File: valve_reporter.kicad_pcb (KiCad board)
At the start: 2 copper layers, 52 parts, among them J1 Screw_Terminal_01x05, J2 Screw_Terminal_01x14, K1 G5LE-1, Q1 2N3904, U1 NodeMCU_1.0_(ESP-12E), U2 MC7805CTG

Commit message: Schematic is shaping up
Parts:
- added H5: MountingHole_Pad, MountingHole:MountingHole_3.2mm_M3_ISO7380_Pad, F.Cu at (136.0, 129.6)
- added H6: MountingHole_Pad, MountingHole:MountingHole_3.2mm_M3_ISO7380_Pad, F.Cu at (110.6, 77.6)
- added H7: MountingHole_Pad, MountingHole:MountingHole_3.2mm_M3_ISO7380_Pad, F.Cu at (136.0, 77.5)
- added H8: MountingHole_Pad, MountingHole:MountingHole_3.2mm_M3_ISO7380_Pad, F.Cu at (110.6, 129.7)
- D3, D4, D5, D6, D7, D8, D9: footprint Diode_SMD:D_SOD-323F -> Diode_SMD:D_SOD-323_HandSoldering
- J1: footprint TerminalBlock_Phoenix:TerminalBlock_Phoenix_PT-1,5-5-5.0-H_1x05_P5.00mm_Horizontal -> TerminalBlock_Phoenix:TerminalBlock_Phoenix_PT-1,5-5-5.0-H_1x05_P5.00mm_Horizontal_valve_rep
- J2: footprint TerminalBlock_Phoenix:TerminalBlock_Phoenix_PT-1,5-14-3.5-H_1x14_P3.50mm_Horizontal -> TerminalBlock_Phoenix:TerminalBlock_Phoenix_PT-1,5-14-3.5-H_1x14_P3.50mm_Horizontal_valve_rep
- moved U2 99.1 mm to (102.9, 121.9), turned to 270 degrees
- moved H2 94.5 mm to (86.4, 134.6)
- moved D1 88.0 mm to (95.2, 134.1), turned to 270 degrees
- moved H3 76.0 mm to (86.4, 73.7)
- moved C9 70.2 mm to (105.4, 134.0), turned to 270 degrees
- moved Q1 69.9 mm to (103.9, 100.7), turned to 180 degrees
- moved R1 68.8 mm to (100.3, 134.0), turned to 90 degrees
- moved R17 68.8 mm to (101.7, 74.9), turned to 180 degrees
- moved R16 68.4 mm to (155.1, 126.3), turned to 180 degrees
- moved R2 67.7 mm to (102.7, 110.5)
- moved C8 64.0 mm to (102.7, 115.6)
- moved J2 56.6 mm to (170.2, 127.0), turned to 90 degrees
- moved J1 55.3 mm to (88.9, 104.8), turned to 270 degrees
- moved R7 46.2 mm to (142.2, 113.0), turned to 90 degrees
- moved D2 45.9 mm to (102.7, 106.7)
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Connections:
- net Net-(J1-Pad3) renamed /RelOn
- net Net-(J1-Pad4) renamed /RelOff
- net Net-(J1-Pad5) renamed /RelIn
- J2 pad 1: +12V -> Net-(D16-Pad1)
- J2 pad 10: Net-(D14-Pad1) -> +12V
- J2 pad 11: +12V -> Net-(D11-Pad1)
- J2 pad 12: Net-(D15-Pad1) -> +12V
- J2 pad 13: +12V -> Net-(D10-Pad1)
- J2 pad 14: Net-(D16-Pad1) -> +12V
- J2 pad 2: Net-(D10-Pad1) -> +12V
- J2 pad 3: +12V -> Net-(D15-Pad1)
- J2 pad 4: Net-(D11-Pad1) -> +12V
- J2 pad 5: +12V -> Net-(D14-Pad1)
- J2 pad 6: Net-(D12-Pad1) -> +12V
- J2 pad 7: +12V -> Net-(D13-Pad1)
- J2 pad 8: Net-(D13-Pad1) -> +12V
- J2 pad 9: +12V -> Net-(D12-Pad1)
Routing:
- net +12V: track 0.00 -> 178.0 mm
- net Net-(C1-Pad1): track 0.00 -> 56.2 mm
- net /RelIn: track 0.00 -> 43.9 mm
- net /RelOff: track 0.00 -> 39.8 mm
- net Net-(R2-Pad2): track 0.00 -> 34.1 mm
- net Net-(C7-Pad1): track 0.00 -> 32.3 mm
- net Net-(D2-Pad2): track 0.00 -> 29.8 mm
- net Net-(C6-Pad1): track 0.00 -> 28.9 mm
- net Net-(C4-Pad1): track 0.00 -> 23.3 mm
- net Net-(C5-Pad1): track 0.00 -> 23.0 mm
- net /RelOn: track 0.00 -> 22.8 mm
- net +5V: track 0.00 -> 21.5 mm
- net Net-(C3-Pad1): track 0.00 -> 20.5 mm
- net Net-(C2-Pad1): track 0.00 -> 17.9 mm
- net Net-(D12-Pad1): track 0.00 -> 15.0 mm
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- added copper zone on B.Cu, net GND
- added copper zone on F.Cu, net GND
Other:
- board outline added: 96.5 x 71.1 mm
- net class Power added: clearance 0.2, trace_width 0.75, via_dia 0.8, via_drill 0.4
- net class Relay added: clearance 0.8, trace_width 1, via_dia 0.8, via_drill 0.4
- board text added: "GSV"
- board text added: "Lou Vervecken 01/19"
- board text added: "Valve Reporter 1.0"

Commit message: Add outputs
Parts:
- added G***: LOGO, artwork:m_vac, F.Cu at (157.5, 74.9)

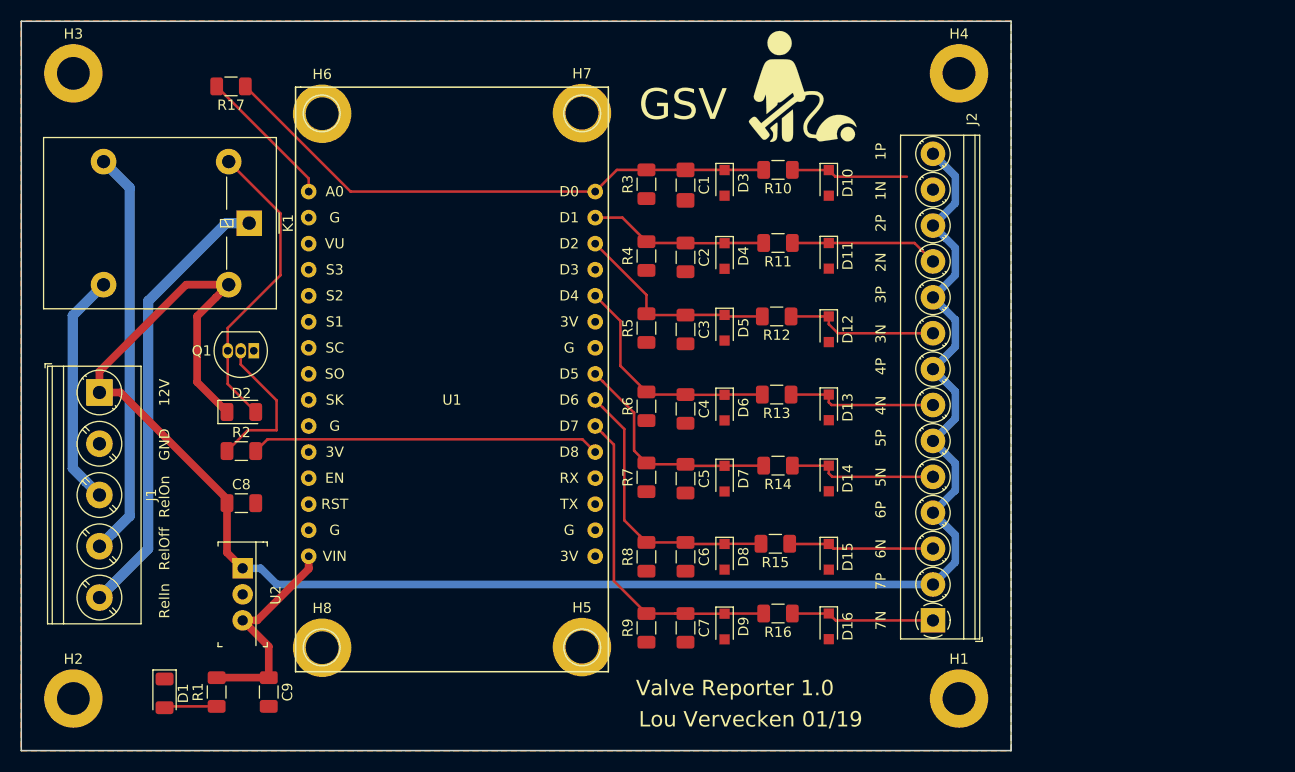
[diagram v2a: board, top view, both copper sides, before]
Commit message: Fixed non connect and increased keepout
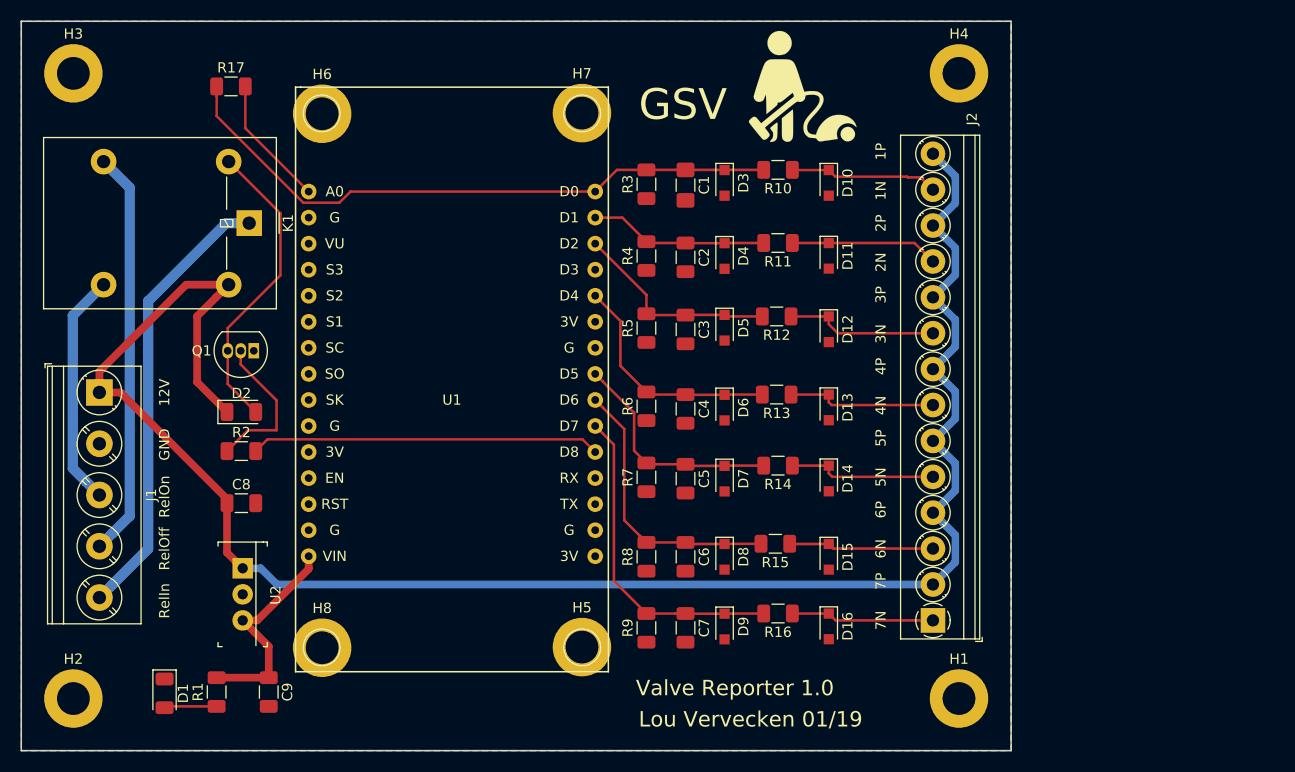
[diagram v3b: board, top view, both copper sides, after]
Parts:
- turned R17 to 0 degrees
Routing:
- net Net-(C1-Pad1): track 56.2 -> 61.6 mm
- net Net-(D10-Pad1): track 11.4 -> 14.5 mm
- net Net-(R17-Pad2): track 14.0 -> 12.8 mm
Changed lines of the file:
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@@
     (thickness 1.6)
     (drawings 7)
-    (tracks 183)
+    (tracks 190)
     (zones 0)
     (modules 57)
@@
   )
   (module Resistor_SMD:R_1206_3216Metric (layer F.Cu)
-    (at 101.73 74.93 180)
+    (at 101.73 74.93)
     (descr "Resistor SMD 1206 (3216 Metric), square (rectangular) end terminal, IPC_7351 nominal, (Body size source: http://www.tortai-tech.com/upload/download/2011102023233369053.pdf), generated with kicad-footprint-generator")
     (tags resistor)
     (attr smd)
-    (fp_text reference R17 (at 0 -1.82 180) (layer F.SilkS)
-      (effects (font (size 1 1) (thickness 0.15)))
-    )
-    (fp_text value 0 (at 0 1.82 180) (layer F.Fab)
-      (effects (font (size 1 1) (thickness 0.15)))
-    )
-    (fp_text user %R (at 0 0 180) (layer F.Fab)
+    (fp_text reference R17 (at 0 -1.82) (layer F.SilkS)
+      (effects (font (size 1 1) (thickness 0.15)))
+    )
+    (fp_text value 0 (at 0 1.82) (layer F.Fab)
+      (effects (font (size 1 1) (thickness 0.15)))
+    )
+    (fp_text user %R (at 0 0) (layer F.Fab)
       (effects (font (size 0.8 0.8) (thickness 0.12)))
     )
@@
     (fp_line (start -1.6 -0.8) (end 1.6 -0.8) (layer F.Fab) (width 0.1))
     (fp_line (start -1.6 0.8) (end -1.6 -0.8) (layer F.Fab) (width 0.1))
-    (pad 2 smd roundrect (at 1.4 0 180) (size 1.25 1.75) (layers F.Cu F.Paste F.Mask) (roundrect_rratio 0.2)
+    (pad 2 smd roundrect (at 1.4 0) (size 1.25 1.75) (layers F.Cu F.Paste F.Mask) (roundrect_rratio 0.2)
       (net 22 "Net-(R17-Pad2)"))
-    (pad 1 smd roundrect (at -1.4 0 180) (size 1.25 1.75) (layers F.Cu F.Paste F.Mask) (roundrect_rratio 0.2)
+    (pad 1 smd roundrect (at -1.4 0) (size 1.25 1.75) (layers F.Cu F.Paste F.Mask) (roundrect_rratio 0.2)
       (net 1 "Net-(C1-Pad1)"))
     (model ${KISYS3DMOD}/Resistor_SMD.3dshapes/R_1206_3216Metric.wrl
@@
   (segment (start 139.360002 83.07) (end 137.245001 85.185001) (width 0.25) (layer F.Cu) (net 1))
   (segment (start 142.24 83.07) (end 139.360002 83.07) (width 0.25) (layer F.Cu) (net 1))
-  (segment (start 113.385001 85.185001) (end 103.13 74.93) (width 0.25) (layer F.Cu) (net 1))
   (segment (start 137.245001 85.185001) (end 113.385001 85.185001) (width 0.25) (layer F.Cu) (net 1))
   (segment (start 149.88 83.07) (end 149.86 83.09) (width 0.25) (layer F.Cu) (net 1))
@@
   (segment (start 149.84 83.07) (end 149.86 83.09) (width 0.25) (layer F.Cu) (net 1))
   (segment (start 146.05 83.07) (end 149.84 83.07) (width 0.25) (layer F.Cu) (net 1))
+  (segment (start 100.33 75.905) (end 100.33 74.93) (width 0.25) (layer F.Cu) (net 1))
+  (segment (start 100.33 77.818762) (end 100.33 75.905) (width 0.25) (layer F.Cu) (net 1))
+  (segment (start 108.78324 86.272002) (end 100.33 77.818762) (width 0.25) (layer F.Cu) (net 1))
+  (segment (start 112.298 86.272002) (end 108.78324 86.272002) (width 0.25) (layer F.Cu) (net 1))
+  (segment (start 113.385001 85.185001) (end 112.298 86.272002) (width 0.25) (layer F.Cu) (net 1))
   (segment (start 150.03 90.2) (end 149.86 90.37) (width 0.25) (layer F.Cu) (net 3))
   (segment (start 146.22 90.37) (end 146.05 90.2) (width 0.25) (layer F.Cu) (net 3))
@@
   (segment (start 156.49 83.09) (end 156.47 83.07) (width 0.25) (layer F.Cu) (net 13))
   (segment (start 160.02 83.09) (end 156.49 83.09) (width 0.25) (layer F.Cu) (net 13))
+  (segment (start 167.710001 83.800001) (end 167.64 83.73) (width 0.25) (layer F.Cu) (net 13))
+  (segment (start 168.980001 83.800001) (end 167.710001 83.800001) (width 0.25) (layer F.Cu) (net 13))
+  (segment (start 170.18 85) (end 168.980001 83.800001) (width 0.25) (layer F.Cu) (net 13))
   (segment (start 168.38 90.2) (end 160.02 90.2) (width 0.25) (layer F.Cu) (net 14))
   (segment (start 170.18 92) (end 168.38 90.2) (width 0.25) (layer F.Cu) (net 14))
@@
   (segment (start 136.007 109.347) (end 137.245001 110.585001) (width 0.25) (layer F.Cu) (net 21))
   (segment (start 105.283 109.347) (end 136.007 109.347) (width 0.25) (layer F.Cu) (net 21))
-  (segment (start 109.305001 83.905001) (end 100.33 74.93) (width 0.25) (layer F.Cu) (net 22))
-  (segment (start 109.305001 85.185001) (end 109.305001 83.905001) (width 0.25) (layer F.Cu) (net 22))
+  (segment (start 103.13 79.01) (end 103.13 74.93) (width 0.25) (layer F.Cu) (net 22))
+  (segment (start 109.305001 85.185001) (end 103.13 79.01) (width 0.25) (layer F.Cu) (net 22))
   (segment (start 87.600001 113.475001) (end 88.9 114.775) (width 1) (layer B.Cu) (net 39))
   (segment (start 86.299999 112.174999) (end 87.600001 113.475001) (width 1) (layer B.Cu) (net 39))
@@
     (polygon
       (pts
-        (xy 114.3 83.82) (xy 114.3 68.58) (xy 132.08 68.58) (xy 132.08 83.82)
+        (xy 109.22 83.82) (xy 109.22 68.58) (xy 137.16 68.58) (xy 137.16 83.82)
       )
     )
-  )
-  (zone (net 2) (net_name GND) (layer F.Cu) (hatch edge 0.508)
-    (connect_pads (clearance 0.508))
-    (min_thickness 0.254)
-    (fill yes (arc_segments 16) (thermal_gap 0.508) (thermal_bridge_width 0.508) (smoothing chamfer))
-    (polygon
-      (pts
-        (xy 81.28 68.58) (xy 81.28 139.7) (xy 177.8 139.7) (xy 177.8 68.58)
-      )
-    )

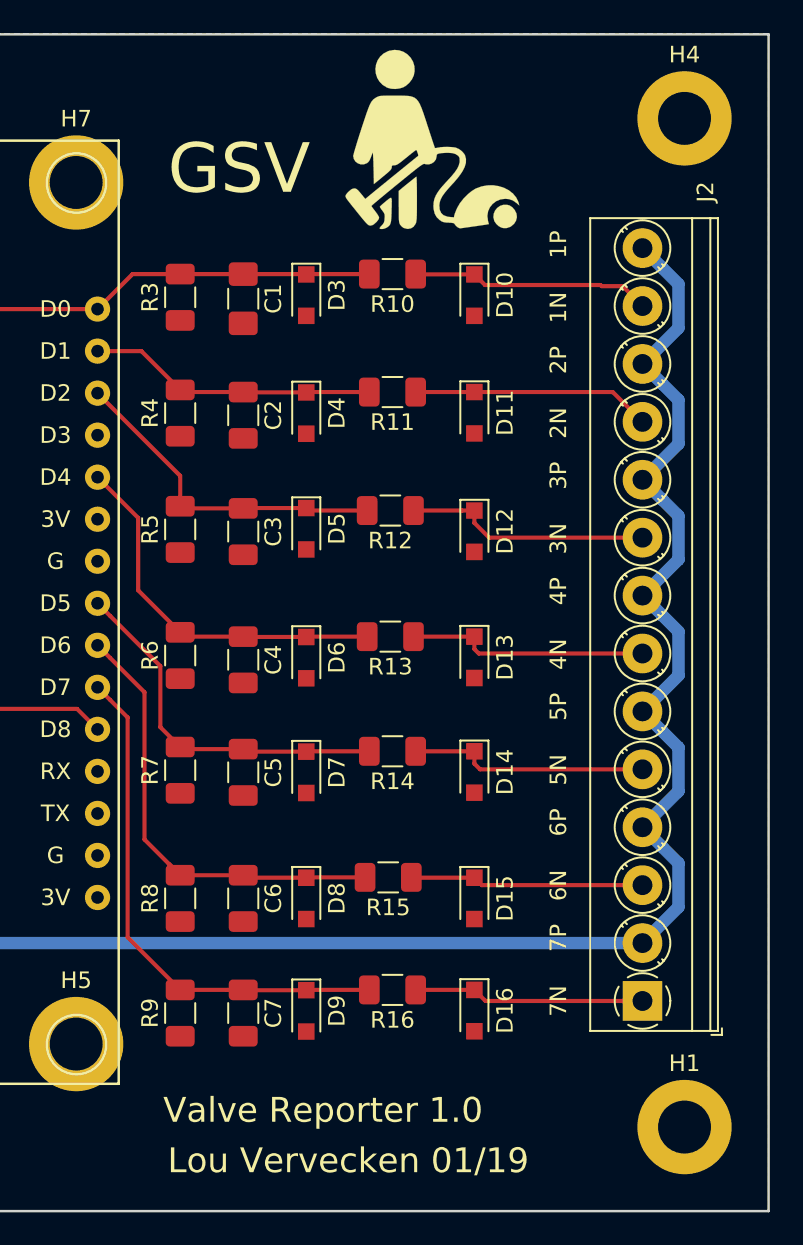
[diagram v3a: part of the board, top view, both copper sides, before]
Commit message: Extra decoupling
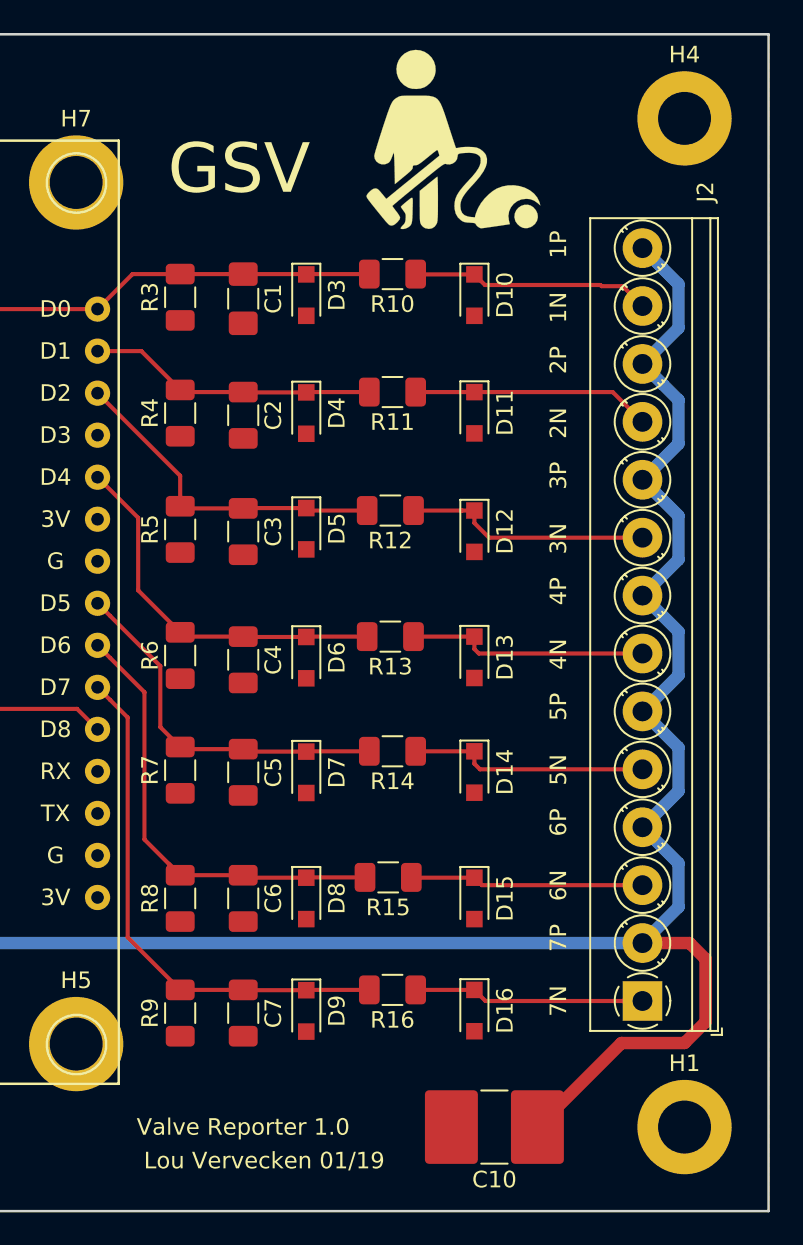
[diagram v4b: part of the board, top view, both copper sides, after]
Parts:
- added C10: 50uF, Capacitor_SMD:C_2816_7142Metric_Pad3.20x4.45mm_HandSolder, F.Cu at (161.2, 134.6)
- moved G*** 1.27 mm to (158.8, 74.9)
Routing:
- net +12V: track 178.0 -> 198.8 mm
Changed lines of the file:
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@@
     (thickness 1.6)
     (drawings 7)
-    (tracks 190)
+    (tracks 196)
     (zones 0)
-    (modules 57)
+    (modules 58)
     (nets 42)
   )
@@
     (add_net /RelOff)
     (add_net /RelOn)
+  )
+  (module Capacitor_SMD:C_2816_7142Metric_Pad3.20x4.45mm_HandSolder (layer F.Cu)
+    (at 161.23 134.62 180)
+    (descr "Capacitor SMD 2816 (7142 Metric), square (rectangular) end terminal, IPC_7351 nominal with elongated pad for handsoldering. (Body size from: https://www.vishay.com/docs/30100/wsl.pdf), generated with kicad-footprint-generator")
+    (tags "capacitor handsolder")
+    (attr smd)
+    (fp_text reference C10 (at 0 -3.18 180) (layer F.SilkS)
+      (effects (font (size 1 1) (thickness 0.15)))
+    )
+    (fp_text value 50uF (at 0 3.18 180) (layer F.Fab)
+      (effects (font (size 1 1) (thickness 0.15)))
+    )
+    (fp_line (start -3.55 2.1) (end -3.55 -2.1) (layer F.Fab) (width 0.1))
+    (fp_line (start -3.55 -2.1) (end 3.55 -2.1) (layer F.Fab) (width 0.1))
+    (fp_line (start 3.55 -2.1) (end 3.55 2.1) (layer F.Fab) (width 0.1))
+    (fp_line (start 3.55 2.1) (end -3.55 2.1) (layer F.Fab) (width 0.1))
+    (fp_line (start -0.797369 -2.21) (end 0.797369 -2.21) (layer F.SilkS) (width 0.12))
+    (fp_line (start -0.797369 2.21) (end 0.797369 2.21) (layer F.SilkS) (width 0.12))
+    (fp_line (start -4.45 2.48) (end -4.45 -2.48) (layer F.CrtYd) (width 0.05))
+    (fp_line (start -4.45 -2.48) (end 4.45 -2.48) (layer F.CrtYd) (width 0.05))
+    (fp_line (start 4.45 -2.48) (end 4.45 2.48) (layer F.CrtYd) (width 0.05))
+    (fp_line (start 4.45 2.48) (end -4.45 2.48) (layer F.CrtYd) (width 0.05))
+    (fp_text user %R (at 0 0 180) (layer F.Fab)
+      (effects (font (size 1 1) (thickness 0.15)))
+    )
+    (pad 1 smd roundrect (at -2.6 0 180) (size 3.2 4.45) (layers F.Cu F.Paste F.Mask) (roundrect_rratio 0.078125)
+      (net 9 +12V))
+    (pad 2 smd roundrect (at 2.6 0 180) (size 3.2 4.45) (layers F.Cu F.Paste F.Mask) (roundrect_rratio 0.078125)
+      (net 2 GND))
+    (model ${KISYS3DMOD}/Capacitor_SMD.3dshapes/C_2816_7142Metric.wrl
+      (at (xyz 0 0 0))
+      (scale (xyz 1 1 1))
+      (rotate (xyz 0 0 0))
+    )
   )
   (module Diode_SMD:D_SOD-323_HandSoldering (layer F.Cu)
@@
   )
   (module artwork:m_vac (layer F.Cu)
-    (at 157.48 74.93)
+    (at 158.75 74.93)
     (fp_text reference G*** (at 0 0) (layer F.SilkS) hide
       (effects (font (size 1.524 1.524) (thickness 0.3)))
@@
       (xy -2.485976 3.533957)) (layer F.SilkS) (width 0.01))
   )
-  (gr_text "Lou Vervecken 01/19" (at 152.4 136.652) (layer F.SilkS)
-    (effects (font (size 1.5 1.5) (thickness 0.3)))
-  )
-  (gr_text "Valve Reporter 1.0" (at 150.876 133.604) (layer F.SilkS)
-    (effects (font (size 1.5 1.5) (thickness 0.3)))
+  (gr_text "Lou Vervecken 01/19" (at 147.32 136.652) (layer F.SilkS)
+    (effects (font (size 1 1) (thickness 0.25)))
+  )
+  (gr_text "Valve Reporter 1.0" (at 146.05 134.62) (layer F.SilkS)
+    (effects (font (size 1 1) (thickness 0.25)))
   )
   (gr_text GSV (at 145.796 76.708) (layer F.SilkS)
@@
   (segment (start 172.355001 86.324999) (end 172.355001 83.675001) (width 0.75) (layer B.Cu) (net 9))
   (segment (start 170.18 88.5) (end 172.355001 86.324999) (width 0.75) (layer B.Cu) (net 9))
+  (segment (start 170.18 123.5) (end 173.03 123.5) (width 0.75) (layer F.Cu) (net 9))
+  (segment (start 173.03 123.5) (end 173.99 124.46) (width 0.75) (layer F.Cu) (net 9))
+  (segment (start 173.99 124.46) (end 173.99 128.27) (width 0.75) (layer F.Cu) (net 9))
+  (segment (start 173.99 128.27) (end 172.72 129.54) (width 0.75) (layer F.Cu) (net 9))
+  (segment (start 168.91 129.54) (end 163.83 134.62) (width 0.75) (layer F.Cu) (net 9))
+  (segment (start 172.72 129.54) (end 168.91 129.54) (width 0.75) (layer F.Cu) (net 9))
   (segment (start 109.305001 121.822631) (end 109.305001 120.745001) (width 0.75) (layer F.Cu) (net 10))
   (segment (start 109.305001 121.979212) (end 109.305001 121.822631) (width 0.75) (layer F.Cu) (net 10))
